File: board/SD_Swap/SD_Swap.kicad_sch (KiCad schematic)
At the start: 22 parts

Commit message: done with sch
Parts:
- removed C?: C, symbol Device:C
- removed D?: LED, symbol Device:LED
- added C10, C11, C12, C4, C5, C6, C7, C8, C9: 0.1u, Capacitor_SMD:C_0603_1608Metric, symbol Device:C_Small
- added C13: 1u, Capacitor_SMD:C_0603_1608Metric, symbol Device:C_Small
- added Q1: Q_Dual_PNP_PNP_E1B1C2E2B2C1, Package_TO_SOT_SMD:SOT-23-6, symbol Device:Q_Dual_PNP_PNP_E1B1C2E2B2C1
- added R10: 10K, Resistor_SMD:R_0603_1608Metric, symbol Device:R
- added R4, R5: 5.1K, Resistor_SMD:R_0603_1608Metric, symbol Device:R
- added R6, R7: 1K, Resistor_SMD:R_0603_1608Metric, symbol Device:R
- added R8, R9: 6.2k, Resistor_SMD:R_0603_1608Metric, symbol Device:R
- added U1: 74LVC2G14, Package_TO_SOT_SMD:SOT-23-6, symbol 74xGxx:74LVC2G14
- added U7: AP2127N-3.3, Package_TO_SOT_SMD:SOT-23, symbol Regulator_Linear:AP2127N-3.3
- C1, C2, C3: renamed from C?; footprint (none) -> Capacitor_SMD:C_0603_1608Metric
- D1: renamed from D?; footprint (none) -> LED_SMD:LED_0603_1608Metric
- D3: renamed from D?; value LED -> POWER; footprint (none) -> LED_SMD:LED_0603_1608Metric
- JP1, JP2, JP3: renamed from JP?; footprint (none) -> Jumper:SolderJumper-2_P1.3mm_Bridged_RoundedPad1.0x1.5mm
- R1, R11, R2, R3: renamed from R?; footprint (none) -> Resistor_SMD:R_0603_1608Metric
- U2: renamed from U?; footprint (none) -> Package_DFN_QFN:VQFN-32-1EP_5x5mm_P0.5mm_EP3.5x3.5mm
- gave numbers to parts that had none: 7
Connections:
- net STAT is gone; now on net +3.3V: JP2.1 (A)
- net +5V: now also C12.1, C13.1, U7.3 (VI)
- net GND: now also U2.24 (SD_WP), C10.2, C11.2, C12.2, C13.2, C4.2, C5.2, C6.2, C7.2, C8.2, C9.2, R10.2, R4.2, R5.2, R8.1, R9.1, U1.2 (GND), U1.2 (GND), U7.1 (GND)
- net SD_SEL: now also R7.2, R8.2, U1.6
- net SS_RX+: now also J1.A11 (RX2+), J1.B11 (RX1+)
- net SS_RX-: now also J1.A10 (RX2-), J1.B10 (RX1-)
- net SS_TX+: now also J1.A2 (TX1+), J1.B2 (TX2+)
- net SS_TX-: now also J1.A3 (TX1-), J1.B3 (TX2-)
- net USB+: now also J1.A6 (D+), J1.B6 (D+)
- net USB-: now also J1.A7 (D-), J1.B7 (D-)
- net VCC: now also Q1.3 (C2), Q1.6 (C1), U1.5 (VCC), U1.5 (VCC); no longer U3.4 (VDD), U4.6 (Vcc)
- net at C1.1, U2.9 (XTLI), Y1.1: now also R10.1
- net at JP3.2 (B): now also R6.2, U1.1, U1.4
- net at U5.13 (NO6): now also U2.22 (SD_D3)
- net at J1.A5 (CC1): now also R5.1
- net at J1.B5 (CC2): now also R4.1
- net +1V2: now reaches U2.11 (USB2_AV12)
- net +1V2: now also U2.25 (DV12S), U2.32 (VDD_RX), U2.5 (USB3_AV12), C10.1, C11.1, C8.1, C9.1
- net +3.3V: now reaches U2.15 (D3V3)
- net +3.3V: now also U2.7 (AV33), U4.6 (Vcc), C4.1, C5.1, C6.1, C7.1, Q1.4 (E2), U7.2 (VO)
- net at U2.16 (CARD_3V3): now also R9.2, U1.3
- new net: Q1.1 (E1), U3.4 (VDD)
- new net: Q1.2 (B1), R7.1
- new net: Q1.5 (B2), R6.1
- no-connect marks 0 -> 2
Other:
- note added: "IDK which one is the PWR out"
- note added: "REFF pin can use a 6.8k. Pulling XTLI low will use the int osc."
- note added: "We cant use PMOS because of the body diode."
- moved on the sheet: D3, JP2, R2

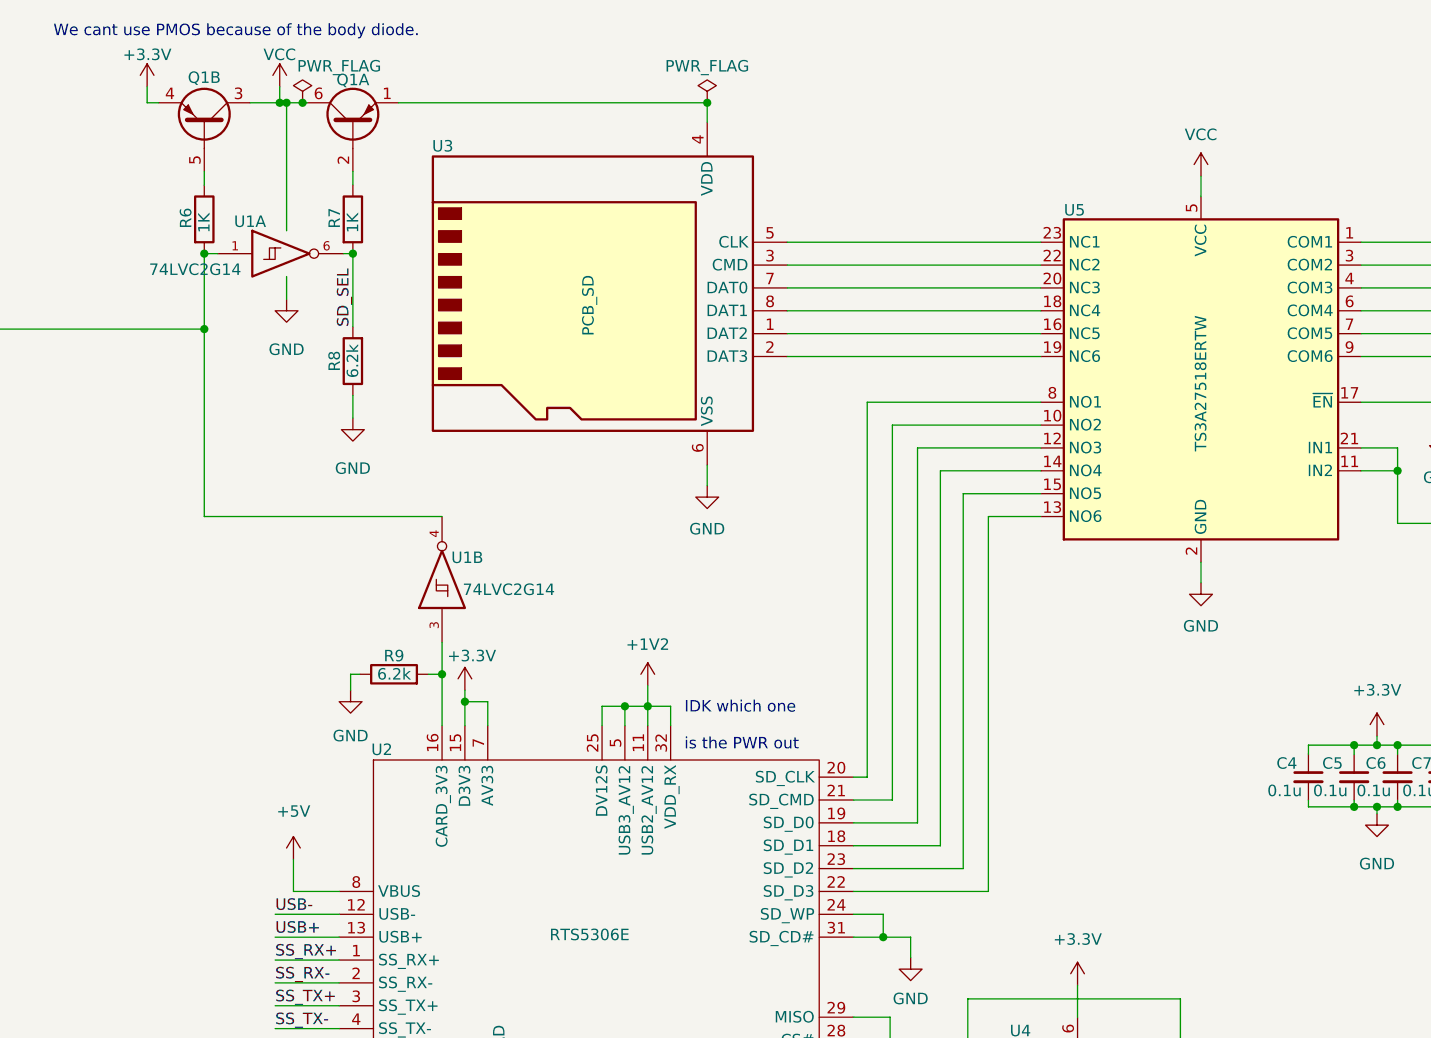
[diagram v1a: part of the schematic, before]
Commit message: working on pcb add some caps to sch
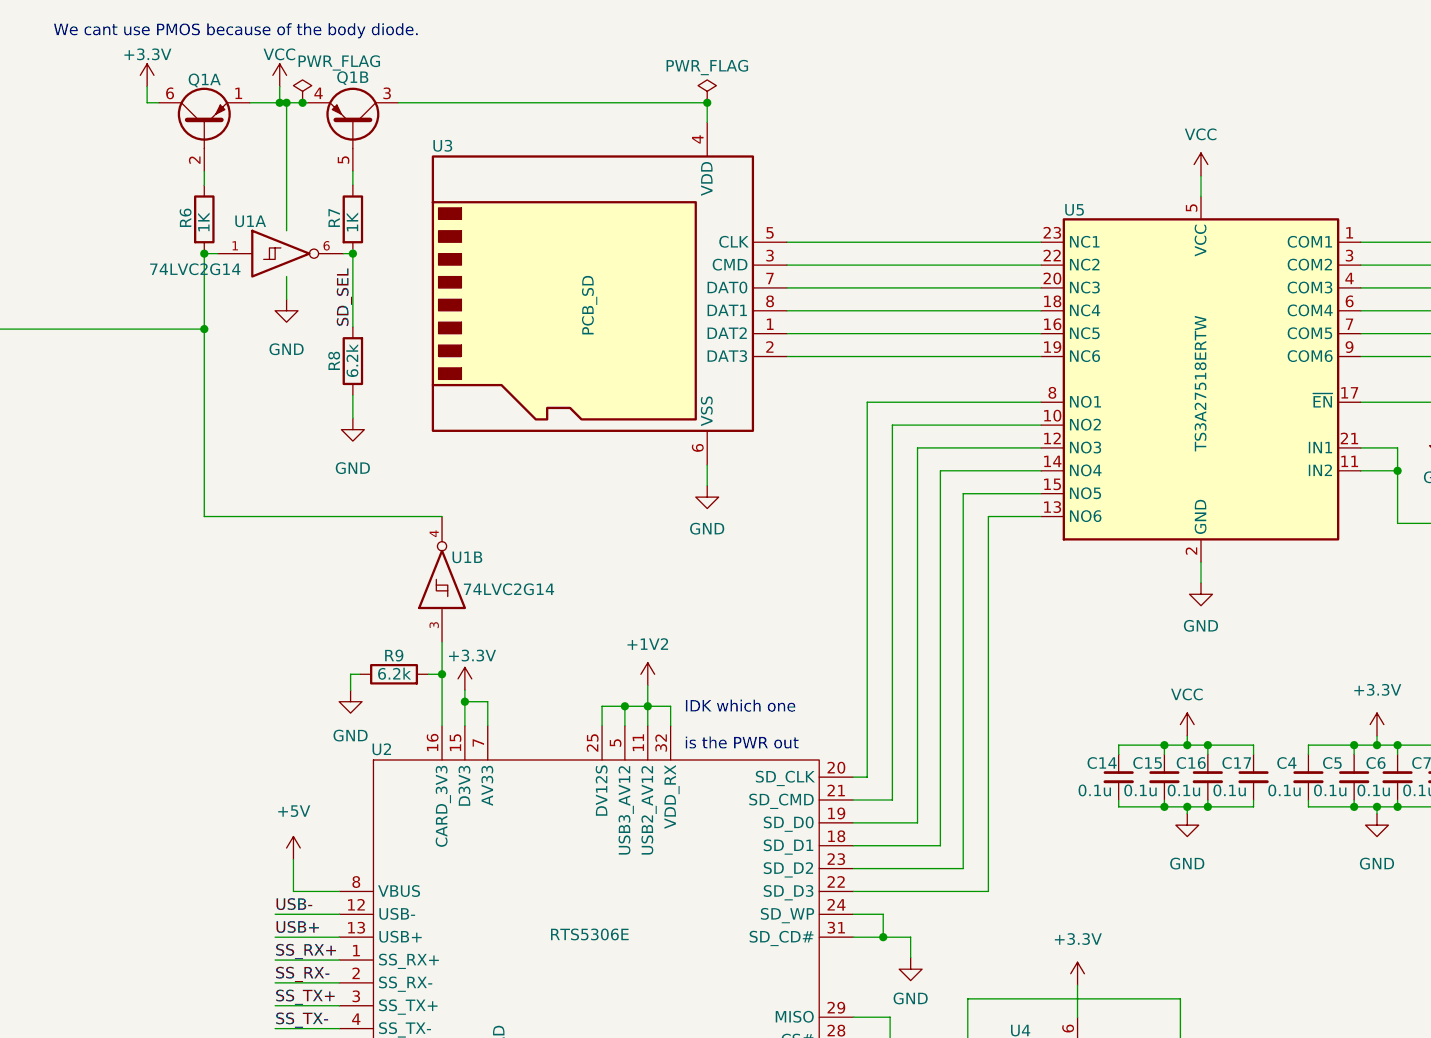
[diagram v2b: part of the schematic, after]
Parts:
- added C14, C15, C16, C17: 0.1u, Capacitor_SMD:C_0603_1608Metric, symbol Device:C_Small
- D2: footprint (none) -> LED_SMD:LED_RGB_1210
- J1: footprint (none) -> Connector_USB:USB_C_Receptacle_Amphenol_12401548E4-2A
- Y1: footprint (none) -> Crystal:Crystal_SMD_Abracon_ABM8G-4Pin_3.2x2.5mm
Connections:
- net +3.3V: now also Q1.6 (C1); no longer Q1.4 (E2)
- net GND: now also C14.2, C15.2, C16.2, C17.2
- net VCC: now also Q1.1 (E1), Q1.4 (E2), C14.1, C15.1, C16.1, C17.1; no longer Q1.3 (C2), Q1.6 (C1)
- net at U3.4 (VDD): now also Q1.3 (C2); no longer Q1.1 (E1)
- net at Q1.2 (B1): now also R6.1; no longer R7.1
- net at Q1.5 (B2): now also R7.1; no longer R6.1
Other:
- moved on the sheet: Q1A, Q1B

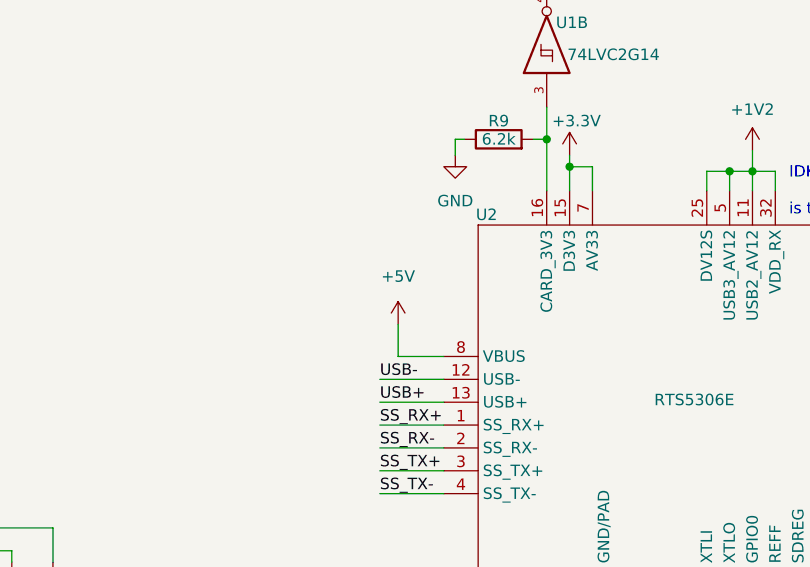
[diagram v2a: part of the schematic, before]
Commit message: mostly done with the usb side of the brd
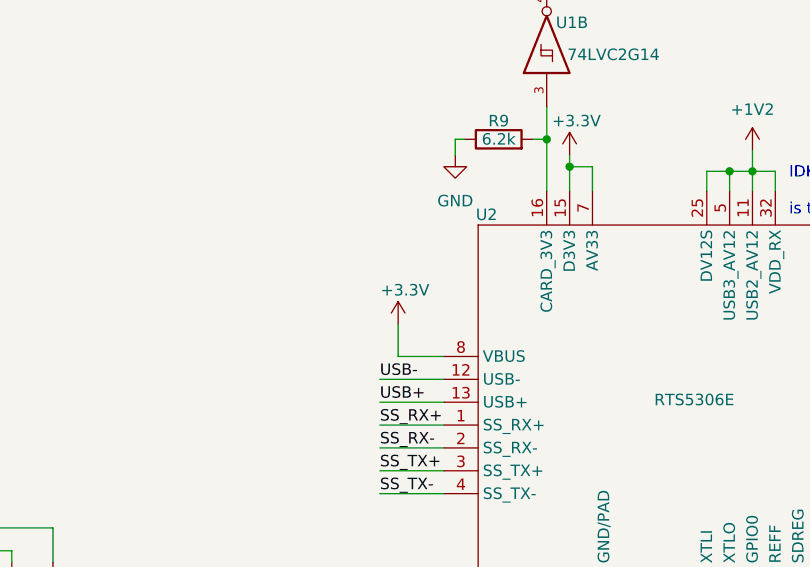
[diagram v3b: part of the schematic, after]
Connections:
- net +3.3V: now also U2.14 (VBUS), U2.8 (VBUS)
- net +5V: no longer U2.14 (VBUS), U2.8 (VBUS)
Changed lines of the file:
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@@
+    (pin "1")
+  )
+  (symbol (lib_id "power:+3.3V") (at 103.124 105.156 0) (unit 1)
+    (in_bom yes) (on_board yes)
+    (property "Reference" "#PWR?" (id 0) (at 103.124 108.966 0)
+      (effects (font (size 1.27 1.27)) hide)
+    )
+    (property "Value" "+3.3V" (id 1) (at 103.886 101.346 0))
+    (property "Footprint" "" (id 2) (at 103.124 105.156 0)
+      (effects (font (size 1.27 1.27)) hide)
+    )
+    (property "Datasheet" "" (id 3) (at 103.124 105.156 0)
+      (effects (font (size 1.27 1.27)) hide)
+    )
     (pin "1")
   )
@@
     (pin "2")
   )
-  (symbol (lib_id "power:+5V") (at 103.124 105.156 0) (unit 1)
-    (in_bom yes) (on_board yes) (fields_autoplaced)
-    (property "Reference" "#PWR0123" (id 0) (at 103.124 108.966 0)
-      (effects (font (size 1.27 1.27)) hide)
-    )
-    (property "Value" "+5V" (id 1) (at 103.124 99.822 0))
-    (property "Footprint" "" (id 2) (at 103.124 105.156 0)
-      (effects (font (size 1.27 1.27)) hide)
-    )
-    (property "Datasheet" "" (id 3) (at 103.124 105.156 0)
-      (effects (font (size 1.27 1.27)) hide)
-    )
-    (pin "1")
-  )
   (symbol (lib_id "Device:C_Small") (at 220.98 96.012 0) (unit 1)
     (in_bom yes) (on_board yes)
@@
       (reference "#PWR0122") (unit 1) (value "GND") (footprint "")
     )
-    (path "/b7800123-409c-4042-bf9b-a784aa27f89a"
-      (reference "#PWR0123") (unit 1) (value "+5V") (footprint "")
-    )
     (path "/ae4a7985-425d-49dc-b334-b8f663b4738e"
       (reference "#PWR0124") (unit 1) (value "GND") (footprint "")
@@
       (reference "#PWR0139") (unit 1) (value "GND") (footprint "")
     )
+    (path "/4afac0e9-ea65-4b62-b7de-e8273bbd2d81"
+      (reference "#PWR?") (unit 1) (value "+3.3V") (footprint "")
+    )
     (path "/09a8b05e-56e6-46dc-90be-1c6b062da039"

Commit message: more sch and swap component sizes
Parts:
- added C18, C19: 0.1u, Capacitor_SMD:C_0201_0603Metric, symbol Device:C_Small
- C10, C11, C12, C14, C15, C16, C17, C3, C4, C5, C6, C7, C8, C9: footprint Capacitor_SMD:C_0603_1608Metric -> Capacitor_SMD:C_0201_0603Metric
- C13: footprint Capacitor_SMD:C_0603_1608Metric -> Capacitor_SMD:C_0402_1005Metric
- R11, R4, R5, R6, R7, R8, R9: footprint Resistor_SMD:R_0603_1608Metric -> Resistor_SMD:R_0201_0603Metric
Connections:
- net SS_TX+: now also C18.1; no longer U2.3 (SS_TX+)
- net SS_TX-: now also C19.1; no longer U2.4 (SS_TX-)
- new net: C18.2, U2.3 (SS_TX+)
- new net: C19.2, U2.4 (SS_TX-)

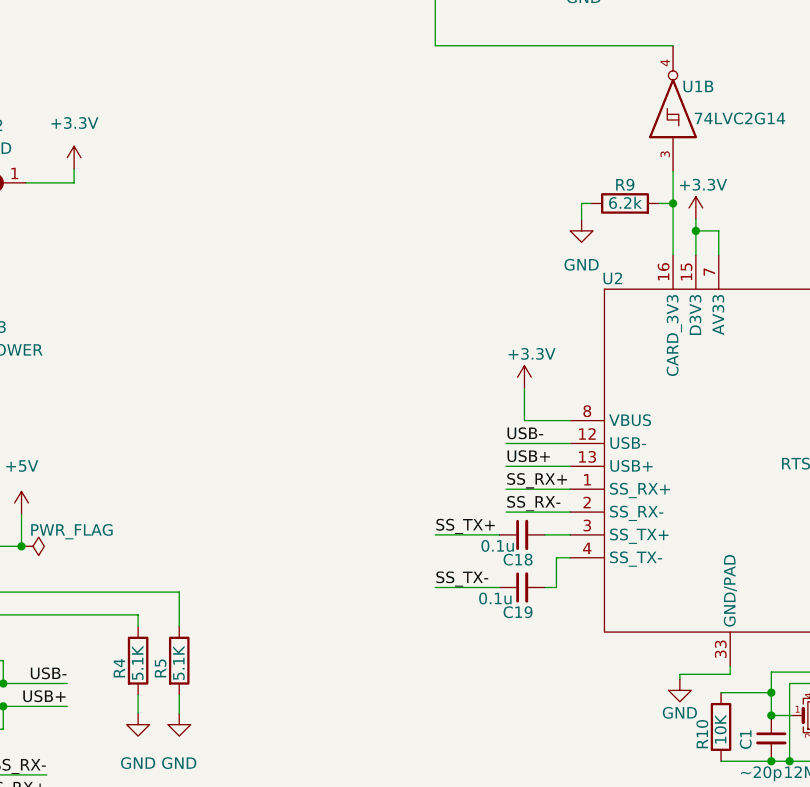
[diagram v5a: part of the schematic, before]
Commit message: add pcb-sd footprint add some notes in the sch
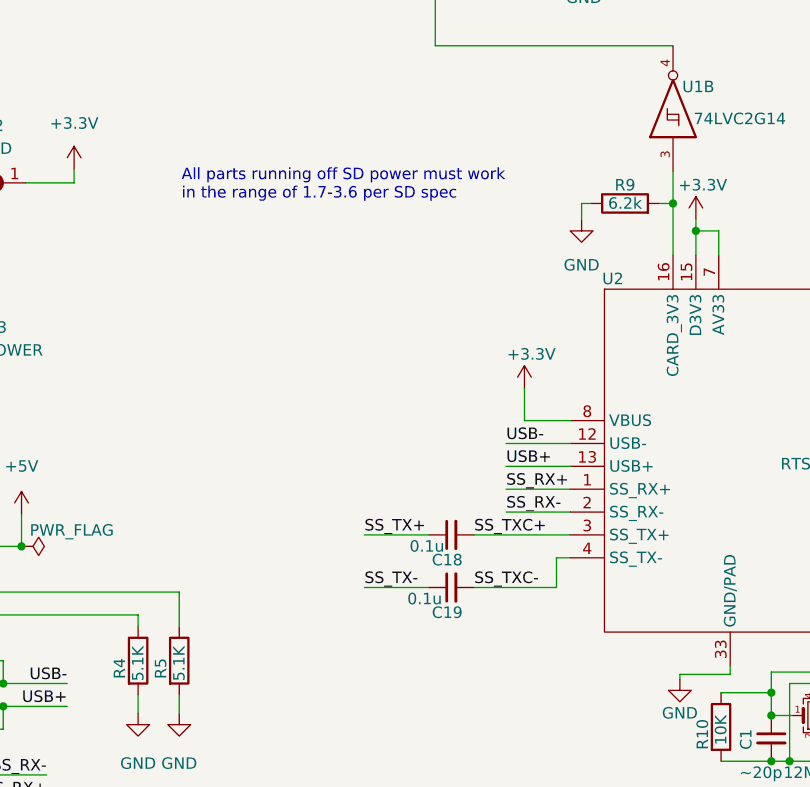
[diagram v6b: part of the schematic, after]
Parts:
- U3: footprint (none) -> SD_Swap:PCB-SD
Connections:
- net SS_TXC+: now reaches C18.2, U2.3 (SS_TX+)
- net SS_TXC-: now reaches C19.2, U2.4 (SS_TX-)
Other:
- note added: "All parts running off SD power must work in the range of 1.7-3.6 per SD spec"
- moved on the sheet: C18, C19
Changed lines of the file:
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@@
     (stroke (width 0) (type default) (color 0 0 0 0))
   )
-  (wire (pts (xy 105.41 127.254) (xy 106.68 127.254))
+  (wire (pts (xy 97.536 127.254) (xy 106.68 127.254))
     (stroke (width 0) (type default) (color 0 0 0 0))
   )
@@
     (stroke (width 0) (type default) (color 0 0 0 0))
   )
-  (wire (pts (xy 93.218 121.412) (xy 100.33 121.412))
+  (wire (pts (xy 85.344 121.412) (xy 92.456 121.412))
     (stroke (width 0) (type default) (color 0 0 0 0))
   )
@@
     (stroke (width 0) (type default) (color 0 0 0 0))
   )
-  (wire (pts (xy 105.41 121.412) (xy 108.204 121.412))
+  (wire (pts (xy 97.536 121.412) (xy 108.204 121.412))
     (stroke (width 0) (type default) (color 0 0 0 0))
   )
@@
     (stroke (width 0) (type default) (color 0 0 0 0))
   )
-  (wire (pts (xy 93.218 127.254) (xy 100.33 127.254))
+  (wire (pts (xy 85.344 127.254) (xy 92.456 127.254))
     (stroke (width 0) (type default) (color 0 0 0 0))
   )
   (text "IDK which one\n\nis the PWR out" (at 146.558 93.218 0)
+    (effects (font (size 1.27 1.27)) (justify left bottom))
+  )
+  (text "All parts running off SD power must work\nin the range of 1.7-3.6 per SD spec"
+    (at 65.024 84.328 0)
     (effects (font (size 1.27 1.27)) (justify left bottom))
   )
@@
     (effects (font (size 1.27 1.27)) (justify left bottom))
   )
-  (label "SS_TX-" (at 93.218 127.254 0)
+  (label "SS_TXC-" (at 97.536 127.254 0)
+    (effects (font (size 1.27 1.27)) (justify left bottom))
+  )
+  (label "SS_TX-" (at 85.344 127.254 0)
     (effects (font (size 1.27 1.27)) (justify left bottom))
   )
@@
     (effects (font (size 1.27 1.27)) (justify left bottom))
   )
-  (label "SS_TX+" (at 93.218 121.412 0)
+  (label "SS_TX+" (at 85.344 121.412 0)
     (effects (font (size 1.27 1.27)) (justify left bottom))
   )
@@
   (label "SD_SEL" (at 236.982 67.818 180)
     (effects (font (size 1.27 1.27)) (justify right bottom))
+  )
+  (label "SS_TXC+" (at 97.536 121.412 0)
+    (effects (font (size 1.27 1.27)) (justify left bottom))
   )
   (symbol (lib_id "Device:C_Small") (at 225.806 96.012 0) (unit 1)
@@
     (pin "1")
   )
-  (symbol (lib_id "Device:C_Small") (at 102.87 121.412 90) (unit 1)
-    (in_bom yes) (on_board yes)
-    (property "Reference" "C18" (id 0) (at 104.14 124.206 90)
-      (effects (font (size 1.27 1.27)) (justify left))
-    )
-    (property "Value" "0.1u" (id 1) (at 102.108 122.682 90)
-      (effects (font (size 1.27 1.27)) (justify left))
-    )
-    (property "Footprint" "Capacitor_SMD:C_0201_0603Metric" (id 2) (at 102.87 121.412 0)
-      (effects (font (size 1.27 1.27)) hide)
-    )
-    (property "Datasheet" "~" (id 3) (at 102.87 121.412 0)
+  (symbol (lib_id "Device:C_Small") (at 94.996 121.412 90) (unit 1)
+    (in_bom yes) (on_board yes)
+    (property "Reference" "C18" (id 0) (at 96.266 124.206 90)
+      (effects (font (size 1.27 1.27)) (justify left))
+    )
+    (property "Value" "0.1u" (id 1) (at 94.234 122.682 90)
+      (effects (font (size 1.27 1.27)) (justify left))
+    )
+    (property "Footprint" "Capacitor_SMD:C_0201_0603Metric" (id 2) (at 94.996 121.412 0)
+      (effects (font (size 1.27 1.27)) hide)
+    )
+    (property "Datasheet" "~" (id 3) (at 94.996 121.412 0)
       (effects (font (size 1.27 1.27)) hide)
     )
@@
       (effects (font (size 1.27 1.27)) (justify left))
     )
-    (property "Footprint" "" (id 2) (at 154.178 27.051 0)
+    (property "Footprint" "SD_Swap:PCB-SD" (id 2) (at 154.178 27.051 0)
       (effects (font (size 1.27 1.27)) hide)
     )
@@
     (pin "1")
   )
-  (symbol (lib_id "Device:C_Small") (at 102.87 127.254 90) (unit 1)
-    (in_bom yes) (on_board yes)
-    (property "Reference" "C19" (id 0) (at 104.14 130.048 90)
-      (effects (font (size 1.27 1.27)) (justify left))
-    )
-    (property "Value" "0.1u" (id 1) (at 101.854 128.524 90)
-      (effects (font (size 1.27 1.27)) (justify left))
-    )
-    (property "Footprint" "Capacitor_SMD:C_0201_0603Metric" (id 2) (at 102.87 127.254 0)
-      (effects (font (size 1.27 1.27)) hide)
-    )
-    (property "Datasheet" "~" (id 3) (at 102.87 127.254 0)
+  (symbol (lib_id "Device:C_Small") (at 94.996 127.254 90) (unit 1)
+    (in_bom yes) (on_board yes)
+    (property "Reference" "C19" (id 0) (at 96.266 130.048 90)
+      (effects (font (size 1.27 1.27)) (justify left))
+    )
+    (property "Value" "0.1u" (id 1) (at 93.98 128.524 90)
+      (effects (font (size 1.27 1.27)) (justify left))
+    )
+    (property "Footprint" "Capacitor_SMD:C_0201_0603Metric" (id 2) (at 94.996 127.254 0)
+      (effects (font (size 1.27 1.27)) hide)
+    )
+    (property "Datasheet" "~" (id 3) (at 94.996 127.254 0)
       (effects (font (size 1.27 1.27)) hide)
     )
@@
     )
     (path "/a7c02123-17d5-4694-a476-4b5d0aa65017"
-      (reference "U3") (unit 1) (value "PCB_SD") (footprint "")
+      (reference "U3") (unit 1) (value "PCB_SD") (footprint "SD_Swap:PCB-SD")
     )
     (path "/d9669532-455b-48e7-a0b0-44d35d5b0a8a"
